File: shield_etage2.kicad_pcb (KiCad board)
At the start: 2 copper layers, 64 parts, among them J1 Conn_01x02, J10 ToF, J11 Moteur, J12 Moteur, J13 butee, J14 butee, J15 Pixy, J16 comm_f3, J2 Conn_01x02, J3 ToF, J4 ToF, J5 ToF, J6 ToF, J7 ToF, J8 ToF, J9 ToF, Q1 BSS138, Q2 BSS138, Q3 BSS138, Q4 BSS138, Q5 BSS138, Q6 BSS138, SW1 SW_Push, U1 74HC164, U2 LM317_TO3, U3 LM317_TO3, U4 LM317_TO3, U5 L293D

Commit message: avancement général du routage
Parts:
- C1, C11, C12, C2, C3, C4, C8, C9, Q1, Q2, Q3, Q4, Q5, Q6, R1, R10, R11, R12, R13, R14, R16, R17, R2, R3, R4, R5, R6, R7, R8, R9, U1: moved to B.Cu
- moved J2 225.2 mm to (245.0, 16.5), turned to 270 degrees
- moved C4 222.4 mm to (242.5, 17.5), turned to 270 degrees
- moved C3 175.4 mm to (211.0, 63.0), turned to 90 degrees
- moved J1 165.6 mm to (207.0, 64.0), turned to 90 degrees
- moved J5 140.4 mm to (99.0, 74.5), turned to 270 degrees
- moved C10 112.6 mm to (27.2, 55.2), turned to 270 degrees
- moved J3 106.8 mm to (87.0, 74.5), turned to 270 degrees
- moved J4 103.6 mm to (93.0, 74.5), turned to 270 degrees
- moved J7 103.3 mm to (111.0, 74.5), turned to 270 degrees
- moved J6 85.8 mm to (105.0, 74.5), turned to 270 degrees
- moved C5 82.9 mm to (77.2, 118.8), turned to 270 degrees
- moved Q3 82.3 mm to (87.5, 96.2), turned to 180 degrees
- moved R7 79.7 mm to (84.2, 96.2), turned to 90 degrees
- moved Q4 77.6 mm to (87.5, 100.2), turned to 180 degrees
- moved R8 74.6 mm to (84.2, 100.2), turned to 90 degrees
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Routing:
- net GND: track 0.00 -> 251.3 mm
- net /F4/NRST: track 0.00 -> 141.6 mm, vias 0 -> 1
- net +2V8: track 0.00 -> 121.8 mm
- net /LevelShifter_ToF_I2C/I2C_SCL_ToF: track 0.00 -> 66.5 mm, vias 0 -> 2
- net /LevelShifter_ToF_I2C/I2C_SDA_ToF: track 0.00 -> 57.9 mm, vias 0 -> 2
- net /LevelShifter_ToF_I2C/I2C_SDA_STM32: track 0.00 -> 51.7 mm
- net +3V3: track 0.00 -> 49.0 mm
- net /LevelShifter_ShiftRegister/STM32_CP: track 0.00 -> 46.2 mm
- net /LevelShifter_ShiftRegister/STM32_DSAB: track 0.00 -> 42.6 mm
- net /LevelShifter_ShiftRegister/ShiftRegister_CP: track 0.00 -> 30.9 mm
- net /ShiftRegister/Reset_ToF_7: track 0.00 -> 24.0 mm
- net /ShiftRegister/Reset_ToF_0: track 0.00 -> 22.5 mm
- net /LevelShifter_ShiftRegister/ShiftRegister_DSAB: track 0.00 -> 19.5 mm
- net /ShiftRegister/Reset_ToF_6: track 0.00 -> 17.5 mm
- net /pixy/SPI_MISO: track 0.00 -> 16.8 mm
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
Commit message: première version du routage complète
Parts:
- removed H1, H2, H3, H4: MountingHole_Pad, MountingHole:MountingHole_2.2mm_M2_Pad
- C13, C14, C6, C7: moved to B.Cu
- moved R15 215.8 mm to (90.5, 148.8), turned to 0 degrees
- moved U2 201.4 mm to (92.8, 143.2), turned to 0 degrees
- moved J2 186.7 mm to (93.8, 126.0)
- moved C4 182.3 mm to (96.8, 127.0)
- moved C13 175.2 mm to (117.0, 131.8), turned to 180 degrees
- moved C14 166.4 mm to (103.5, 126.2)
- moved U5 161.8 mm to (117.5, 121.8), turned to 270 degrees
- moved C1 150.3 mm to (91.5, 130.8)
- moved C2 146.1 mm to (91.0, 123.5), turned to 0 degrees
- moved R14 145.1 mm to (106.7, 105.2), turned to 0 degrees
- moved R10 144.1 mm to (92.2, 132.8), turned to 180 degrees
- moved R9 143.8 mm to (91.5, 127.2), turned to 90 degrees
- moved Q6 143.1 mm to (110.9, 105.2), turned to 180 degrees
- moved R16 143.0 mm to (84.5, 116.7), turned to 90 degrees
- moved R17 142.7 mm to (91.0, 121.5), turned to 180 degrees
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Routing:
- net GND: track 251.3 -> 487.7 mm
- net +5V: track 12.0 -> 129.6 mm, vias 0 -> 1
- net /LevelShifter_ToF_I2C/I2C_SCL_STM32: track 2.65 -> 82.5 mm, vias 0 -> 2
- net +3V3: track 49.0 -> 98.0 mm, vias 0 -> 2
- net /Driver_moteurs/bras_sens_inverse: track 0.00 -> 45.4 mm
- net +2V8: track 121.8 -> 167.2 mm, vias 0 -> 2
- net /F4/bras_PWM: track 0.00 -> 41.4 mm
- net /Driver_moteurs/drapeau_sens_direct: track 0.00 -> 39.1 mm
- net Net-(C14-Pad2): track 0.00 -> 33.1 mm
- net /F4/drapeau_PWM: track 0.00 -> 33.0 mm
- net Net-(Q6-Pad3): track 0.00 -> 30.9 mm
- net /Driver_moteurs/bras_sens_direct: track 0.00 -> 29.0 mm
- net Net-(Q5-Pad3): track 0.00 -> 26.8 mm
- net /UART_comm_f3/TX: track 0.00 -> 25.5 mm, vias 0 -> 1
- net /Driver_moteurs/drapeau_sens_inverse: track 0.00 -> 24.4 mm
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- added copper zone on B.Cu, net GND

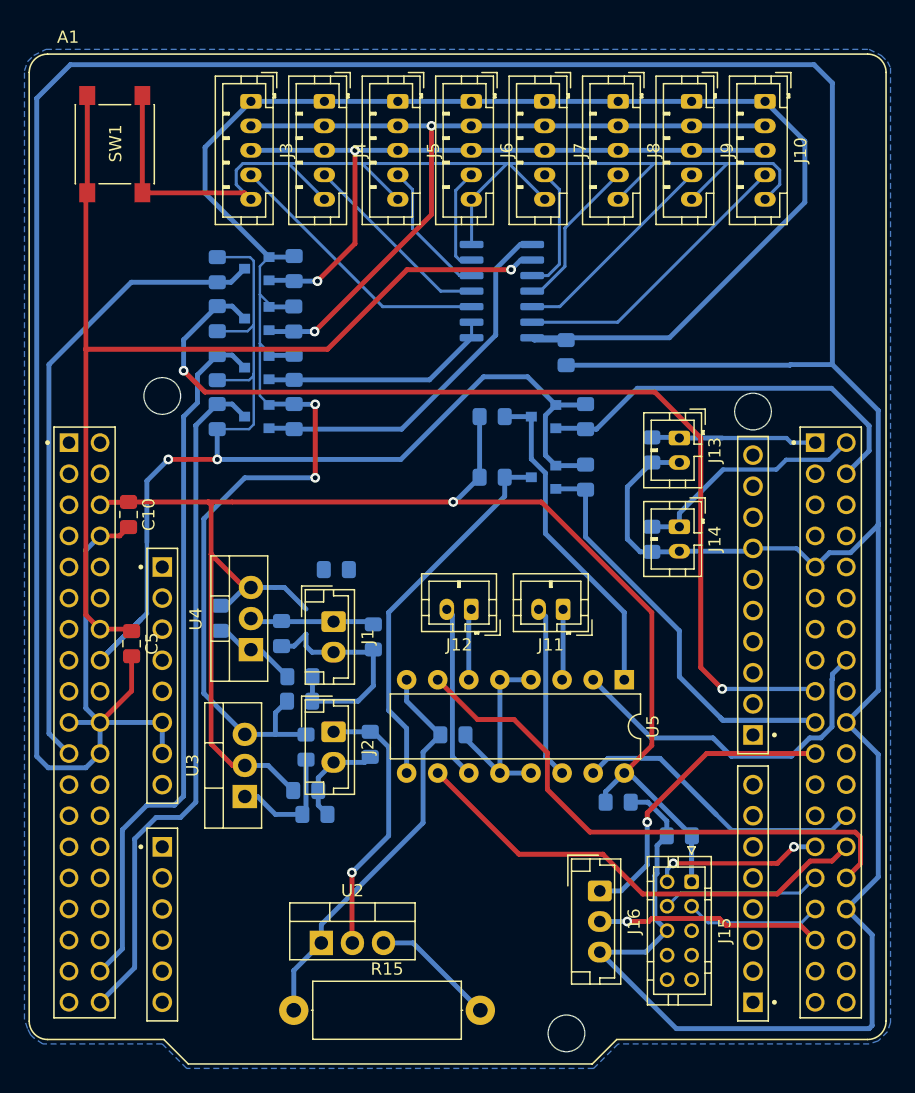
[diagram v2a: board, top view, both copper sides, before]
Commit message: Correction de défauts, quelques pistes refaites plus proprement
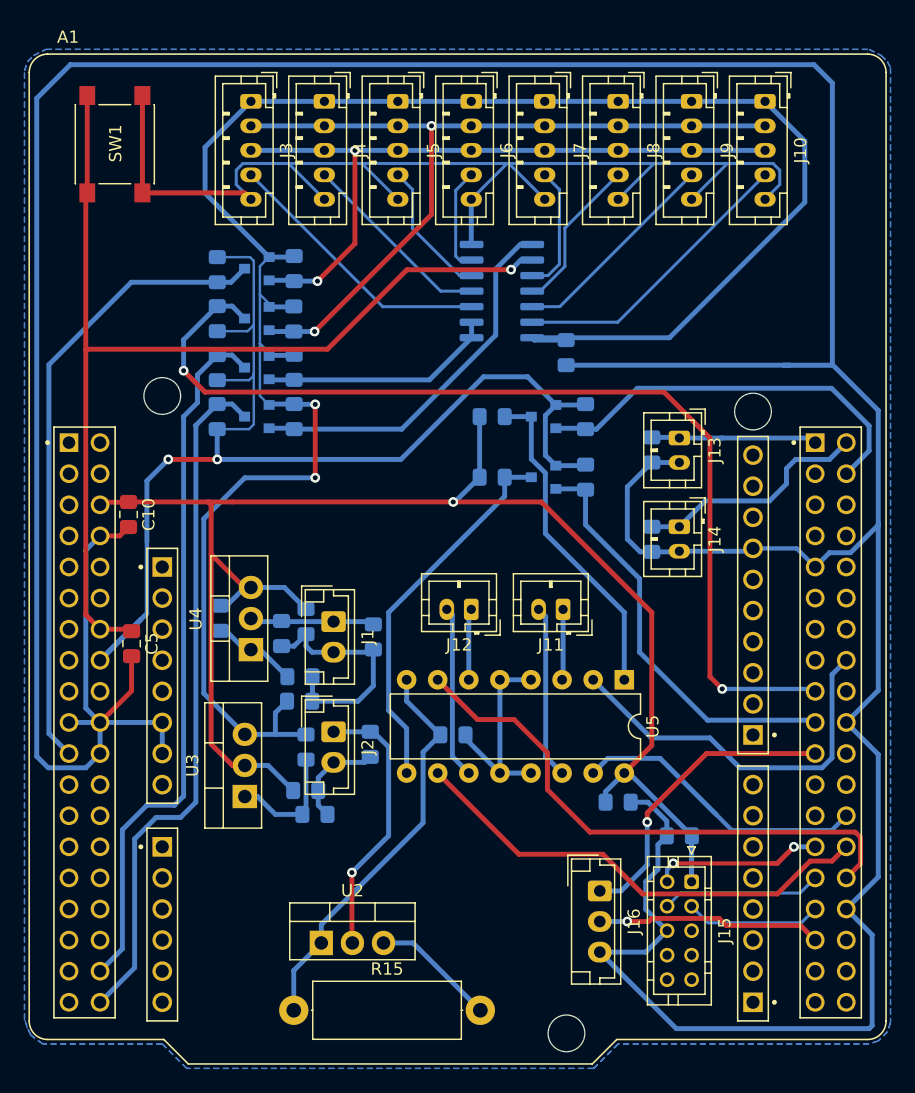
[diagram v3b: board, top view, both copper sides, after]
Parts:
- moved C9 4.92 mm to (91.5, 117.0), turned to 270 degrees
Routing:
- net /F4/bras_PWM: track 41.4 -> 34.3 mm
- net GND: track 487.7 -> 492.2 mm
- net /Driver_moteurs/bras_sens_direct: track 29.0 -> 31.3 mm
